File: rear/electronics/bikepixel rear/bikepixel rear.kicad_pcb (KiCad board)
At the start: 2 copper layers, 80 x 20.1 mm, 21 parts, among them J1 Power, J2 Arduino, J3 Matrix, SW0 on/off, SW1 mode, SW2 color, SW3 effect

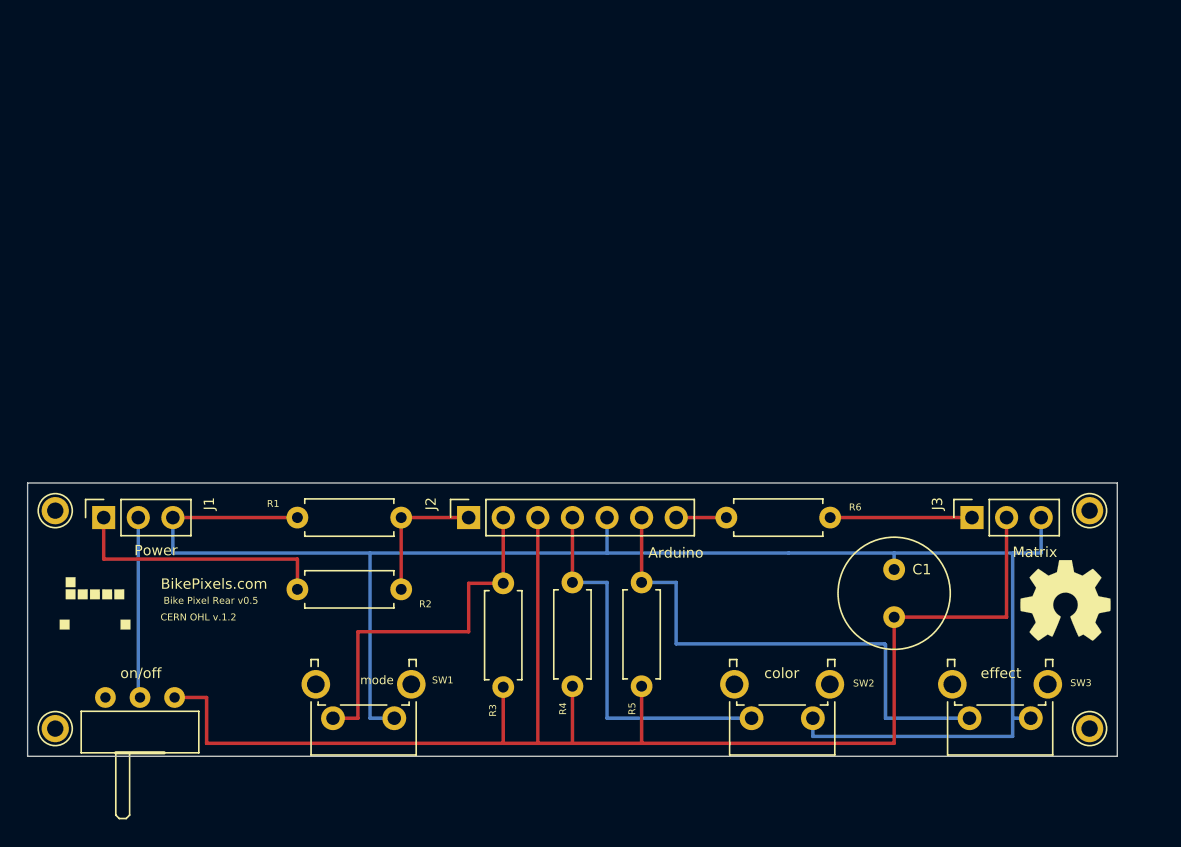
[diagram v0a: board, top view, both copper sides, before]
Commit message: Added files for bike pixel rear with battery support and 3d printed case
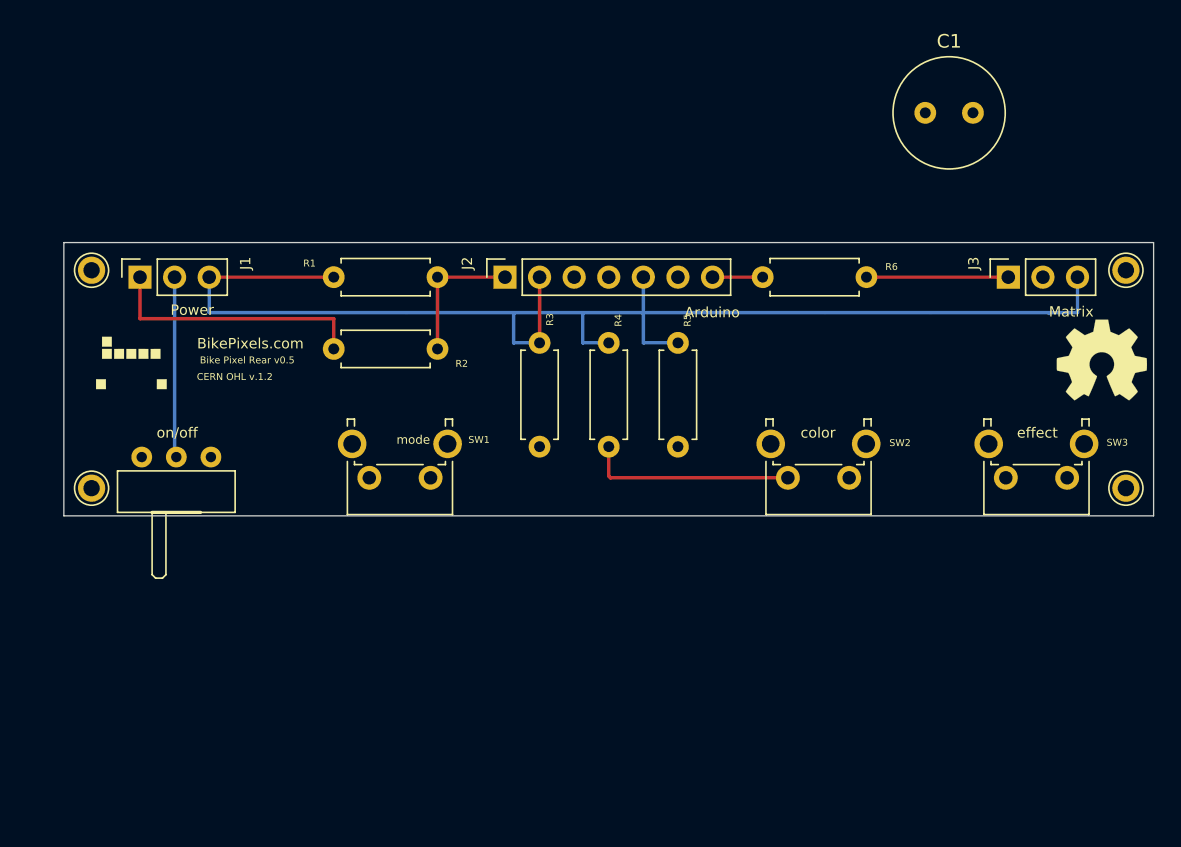
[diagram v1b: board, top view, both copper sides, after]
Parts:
- moved C1 33.6 mm to (167.5, 79.8), turned to 0 degrees
- moved R3 25.4 mm to (139.2, 96.6), turned to 270 degrees
- moved R4 25.4 mm to (144.3, 96.6), turned to 270 degrees
- moved R5 25.4 mm to (149.4, 96.6), turned to 270 degrees
- moved Bike Pixel Rear v0.5 17.9 mm to (109.2, 98.1)
- moved H2 17.9 mm to (106.3, 107.3)
- moved H3 17.9 mm to (182.2, 107.3)
- moved J1 17.9 mm to (109.9, 91.8)
- moved J3 17.9 mm to (173.6, 91.8)
- moved R1 17.9 mm to (124.1, 91.8)
- moved R2 17.9 mm to (124.1, 97.1)
- moved R6 17.9 mm to (155.6, 91.8)
- moved SW0 17.9 mm to (112.5, 105.0)
- moved SW1 17.9 mm to (131.2, 106.6)
- moved SW2 17.9 mm to (161.9, 106.6)
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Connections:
- J2 pad 2: Net-(J2-Pad2) -> (no net)
- J2 pad 4: Net-(J2-Pad4) -> (no net)
- J2 pad 6: Net-(J2-Pad6) -> (no net)
- R3 pad 1: +5V -> GND
- R3 pad 2: Net-(J2-Pad2) -> Net-(R3-Pad2)
- R4 pad 1: +5V -> GND
- R4 pad 2: Net-(J2-Pad4) -> Net-(R4-Pad2)
- R5 pad 1: +5V -> GND
- R5 pad 2: Net-(J2-Pad6) -> Net-(R5-Pad2)
- SW1 pad 1: GND -> +5V
- SW1 pad 2: Net-(J2-Pad2) -> Net-(R3-Pad2)
- SW2 pad 1: GND -> +5V
- SW2 pad 2: Net-(J2-Pad4) -> Net-(R4-Pad2)
- SW3 pad 1: GND -> +5V
- SW3 pad 2: Net-(J2-Pad6) -> Net-(R5-Pad2)
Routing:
- net +5V: track 111.1 -> 0.72 mm
- net Net-(J2-Pad6): track 41.2 -> 0.00 mm
- net GND: track 127.4 -> 98.8 mm
- net Net-(J2-Pad4): track 27.9 -> 0.00 mm
- net Net-(J2-Pad2): track 27.2 -> 0.00 mm
- net Net-(R4-Pad2): track 0.00 -> 15.4 mm
- net Net-(R5-Pad2): track 0.00 -> 2.16 mm

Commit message: Added PCB design. Improved documentation
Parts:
- removed Bike Pixel Rear v0.5: BikePixels.com, Logo:bikepixels_logo_black_part_silk_05mm
- removed CERN OHL v.1.2: Bike Pixels, Logo:bikepixels_logo_red_part_solder_05mm
- removed H1: H1, Connector_Pin:Pin_D1.0mm_L10.0mm
- removed H2: H2, Connector_Pin:Pin_D1.0mm_L10.0mm
- removed H3: H3, Connector_Pin:Pin_D1.0mm_L10.0mm
- removed H4: H4, Connector_Pin:Pin_D1.0mm_L10.0mm
- added CERN OHL v1.2: Bike Pixel L v0.5, Logo:bikepixels_logo_black_part_silk_05mm, F.Cu at (109.3, 98.2)
- added K. Stopa © 2021: BikePixels.com, Logo:bikepixels_logo_red_part_solder_05mm, F.Cu at (109.3, 98.9)
- moved C1 15.9 mm to (167.6, 95.6), turned to 270 degrees
- moved R3 7.49 mm to (139.2, 104.1), turned to 90 degrees
- moved R4 7.49 mm to (144.3, 104.1), turned to 90 degrees
- moved R5 7.49 mm to (149.4, 104.1), turned to 90 degrees
- moved OSHW 0.54 mm to (180.1, 98.3)
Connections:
- J2 pad 2: (no net) -> Net-(J2-Pad2)
- J2 pad 4: (no net) -> Net-(J2-Pad4)
- J2 pad 6: (no net) -> Net-(J2-Pad6)
- R3 pad 1: GND -> +5V
- R3 pad 2: Net-(R3-Pad2) -> Net-(J2-Pad2)
- R4 pad 1: GND -> +5V
- R4 pad 2: Net-(R4-Pad2) -> Net-(J2-Pad4)
- R5 pad 1: GND -> +5V
- R5 pad 2: Net-(R5-Pad2) -> Net-(J2-Pad6)
- SW1 pad 1: +5V -> GND
- SW1 pad 2: Net-(R3-Pad2) -> Net-(J2-Pad2)
- SW2 pad 1: +5V -> GND
- SW2 pad 2: Net-(R4-Pad2) -> Net-(J2-Pad4)
- SW3 pad 1: +5V -> GND
- SW3 pad 2: Net-(R5-Pad2) -> Net-(J2-Pad6)
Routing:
- net +5V: track 0.72 -> 110.7 mm
- net Net-(J2-Pad6): track 0.00 -> 41.0 mm
- net GND: track 98.8 -> 127.0 mm
- net Net-(J2-Pad4): track 0.00 -> 28.1 mm
- net Net-(J2-Pad2): track 0.00 -> 27.2 mm
- net Net-(R4-Pad2): track 15.4 -> 0.00 mm
- net Net-(R5-Pad2): track 2.16 -> 0.00 mm
